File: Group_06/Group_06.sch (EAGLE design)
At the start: 18 parts, among them J1 POWER_JACKPTH_LOCK, U2 +12v

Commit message: CY8
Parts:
- added D1: BLUE, SparkFun-LED:LED-BLUE1206
- added J3: (no value), SparkFun-Connectors:CONN_06LOCK
- added R11: (no value), SparkFun-Resistors:RESISTORAXIAL-0.3
- added U$2: CY8CKIT-059_TARGET_3, CY8KIT-059:CY8CKIT-059_TARGET_3
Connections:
- new net MUX_A0/2.3C: U$2.P_1.7
- new net MUX_A1/2.3C: U$2.P_1.6
- new net MUX_A2/2.3C: U$2.P_1.5
- new net MUX_OUT/2.5C: U$2.P_1.4
- new net N$2: D1.C, R11.2
- new net N$3: D1.A, U$2.P_3.0
- new net N$4: J3.6, U$2.P_0.0
- new net N$5: J3.5, U$2.P_0.1
- new net N$6: J3.4, U$2.P_0.2
- new net N$7: J3.3, U$2.P_0.3
- new net N$8: J3.2, U$2.P_0.4
- new net N$9: J3.1, U$2.P_0.5
- net 5V: now also U$2.VDD, U$2.VDDIO
- net GND: now also R11.1, U$2.GND1, U$2.GND3
- net I2C_A0: now also U$2.P_2.5
- net I2C_A1: now also U$2.P_2.6
- net I2C_A2: now also U$2.P_2.7
- net I2C_SCL: now also U$2.P_12.0
- net I2C_SDA: now also U$2.P_12.1
- net PHOTO_OUT: now also U$2.P_3.7
- net TEMP_OUT: now also U$2.P_15.0

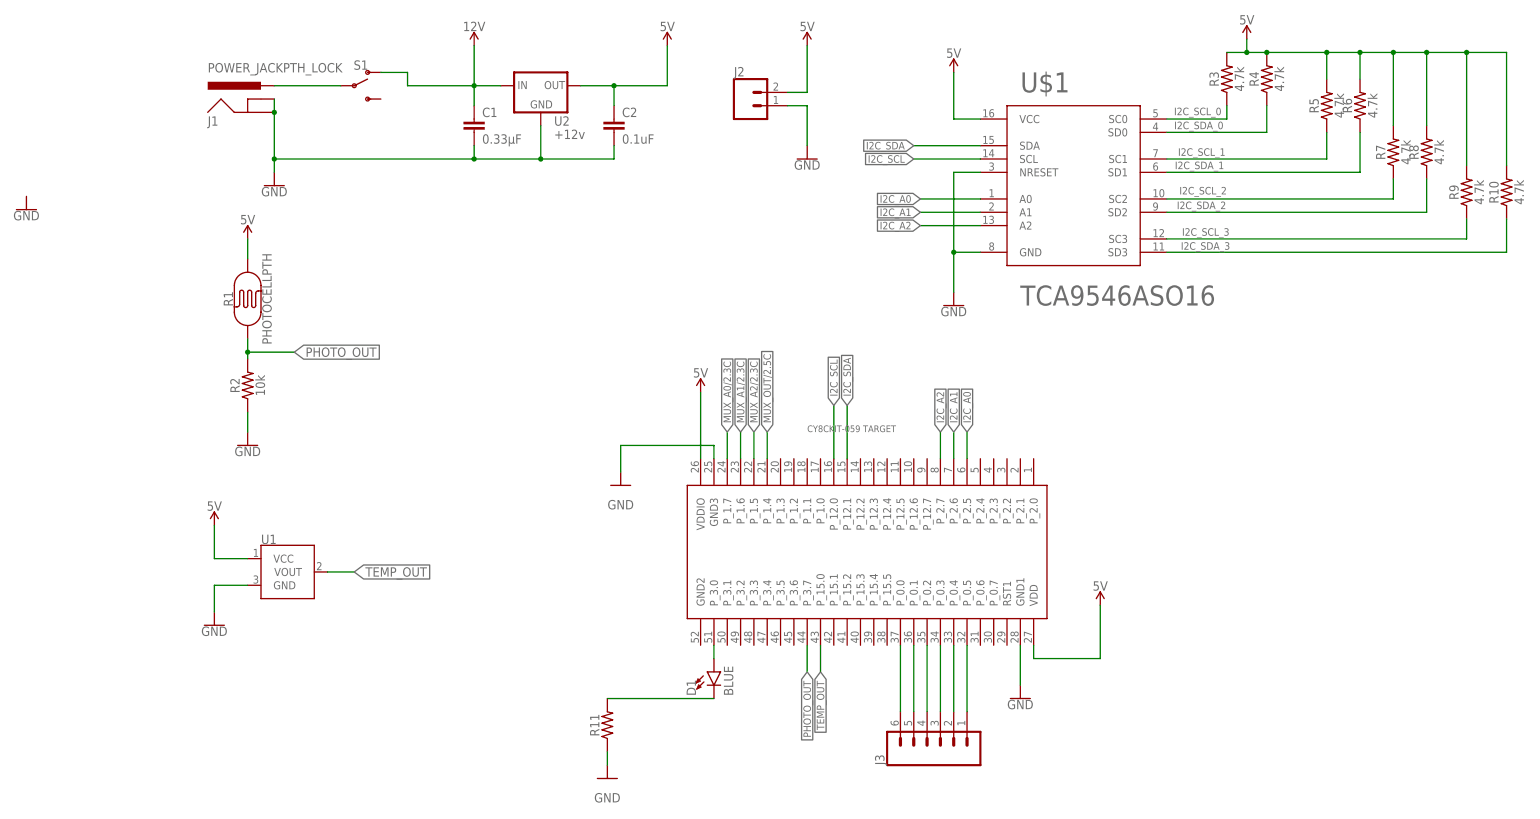
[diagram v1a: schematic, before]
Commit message: I2C_Connectors and Names
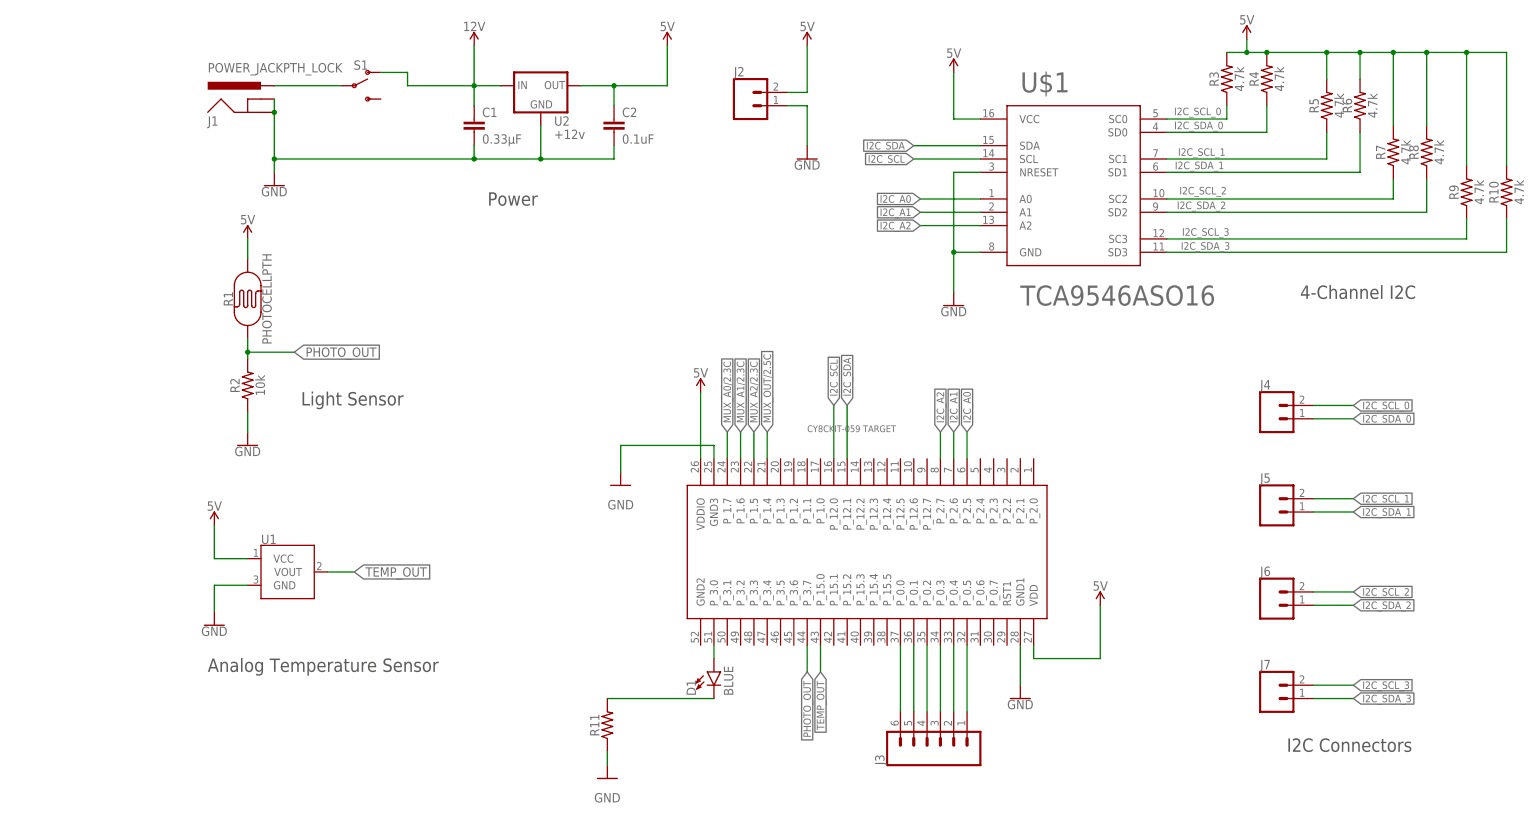
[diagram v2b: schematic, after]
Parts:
- added J4, J5, J6, J7: (no value), SparkFun-Connectors:CONN_02
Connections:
- net I2C_SCL_0: now also J4.2
- net I2C_SCL_1: now also J5.2
- net I2C_SCL_2: now also J6.2
- net I2C_SCL_3: now also J7.2
- net I2C_SDA_0: now also J4.1
- net I2C_SDA_1: now also J5.1
- net I2C_SDA_2: now also J6.1
- net I2C_SDA_3: now also J7.1
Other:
- note added: "4-Channel I2C"
- note added: "Analog Temperature Sensor"
- note added: "I2C Connectors"
- note added: "Light Sensor"
- note added: "Power"
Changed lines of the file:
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@@
 <part name="U$2" library="CY8KIT-059" deviceset="CY8CKIT-059_TARGET_3" device=""/>
 <part name="R11" library="SparkFun-Resistors" deviceset="RESISTOR" device="AXIAL-0.3" value=" "/>
-<part name="GND6" library="SparkFun-PowerSymbols" deviceset="GND" device=""/>
 <part name="GND7" library="SparkFun-PowerSymbols" deviceset="GND" device=""/>
 <part name="GND8" library="SparkFun-PowerSymbols" deviceset="GND" device=""/>
@@
 <part name="D1" library="SparkFun-LED" deviceset="LED-BLUE" device="1206" value="BLUE"/>
 <part name="J3" library="SparkFun-Connectors" deviceset="CONN_06" device="LOCK"/>
+<part name="J4" library="SparkFun-Connectors" deviceset="CONN_02" device=""/>
+<part name="J5" library="SparkFun-Connectors" deviceset="CONN_02" device=""/>
+<part name="J6" library="SparkFun-Connectors" deviceset="CONN_02" device=""/>
+<part name="J7" library="SparkFun-Connectors" deviceset="CONN_02" device=""/>
 </parts>
 <sheets>
 <sheet>
 <plain>
+<text x="223.52" y="35.56" size="2.54" layer="97">I2C Connectors</text>
+<text x="226.06" y="121.92" size="2.54" layer="97">4-Channel I2C</text>
+<text x="71.12" y="139.7" size="2.54" layer="97">Power</text>
+<text x="35.56" y="101.6" size="2.54" layer="97">Light Sensor</text>
+<text x="17.78" y="50.8" size="2.54" layer="97">Analog Temperature Sensor</text>
 </plain>
 <instances>
@@
 <attribute name="VALUE" x="92.964" y="40.64" size="1.778" layer="96" font="vector" rot="R90" align="top-center"/>
 </instance>
-<instance part="GND6" gate="1" x="-16.78295625" y="138.935128125" smashed="yes">
-<attribute name="VALUE" x="-16.78295625" y="138.681128125" size="1.778" layer="96" align="top-center"/>
-</instance>
 <instance part="GND7" gate="1" x="93.98" y="30.48" smashed="yes">
 <attribute name="VALUE" x="93.98" y="27.686" size="1.778" layer="96" align="top-center"/>
@@
 <attribute name="VALUE" x="167.386" y="33.02" size="1.778" layer="96" font="vector" rot="R90"/>
 <attribute name="NAME" x="146.812" y="33.02" size="1.778" layer="95" font="vector" rot="R90"/>
+</instance>
+<instance part="J4" gate="G$1" x="220.98" y="99.06" smashed="yes">
+<attribute name="VALUE" x="218.44" y="94.234" size="1.778" layer="96" font="vector"/>
+<attribute name="NAME" x="218.44" y="104.648" size="1.778" layer="95" font="vector"/>
+</instance>
+<instance part="J5" gate="G$1" x="220.98" y="81.28" smashed="yes">
+<attribute name="VALUE" x="218.44" y="76.454" size="1.778" layer="96" font="vector"/>
+<attribute name="NAME" x="218.44" y="86.868" size="1.778" layer="95" font="vector"/>
+</instance>
+<instance part="J6" gate="G$1" x="220.98" y="63.5" smashed="yes">
+<attribute name="VALUE" x="218.44" y="58.674" size="1.778" layer="96" font="vector"/>
+<attribute name="NAME" x="218.44" y="69.088" size="1.778" layer="95" font="vector"/>
+</instance>
+<instance part="J7" gate="G$1" x="220.98" y="45.72" smashed="yes">
+<attribute name="VALUE" x="218.44" y="40.894" size="1.778" layer="96" font="vector"/>
+<attribute name="NAME" x="218.44" y="51.308" size="1.778" layer="95" font="vector"/>
 </instance>
 </instances>
@@
 <label x="211.074" y="158.369" size="1.4224" layer="95" rot="R180"/>
 </segment>
+<segment>
+<pinref part="J4" gate="G$1" pin="2"/>
+<wire x1="228.6" y1="101.6" x2="236.22" y2="101.6" width="0.1524" layer="91"/>
+<label x="236.22" y="101.6" size="1.4224" layer="95" xref="yes"/>
+</segment>
 </net>
 <net name="I2C_SDA_0" class="0">
@@
 <label x="211.455" y="155.702" size="1.4224" layer="95" rot="R180"/>
 </segment>
+<segment>
+<pinref part="J4" gate="G$1" pin="1"/>
+<wire x1="228.6" y1="99.06" x2="236.22" y2="99.06" width="0.1524" layer="91"/>
+<label x="236.22" y="99.06" size="1.4224" layer="95" xref="yes"/>
+</segment>
 </net>
 <net name="I2C_SCL_1" class="0">
@@
 <label x="211.836" y="150.622" size="1.4224" layer="95" rot="R180"/>
 </segment>
+<segment>
+<pinref part="J5" gate="G$1" pin="2"/>
+<wire x1="228.6" y1="83.82" x2="236.22" y2="83.82" width="0.1524" layer="91"/>
+<label x="236.22" y="83.82" size="1.4224" layer="95" xref="yes"/>
+</segment>
 </net>
 <net name="I2C_SDA_1" class="0">
@@
 <label x="211.582" y="148.082" size="1.4224" layer="95" rot="R180"/>
 </segment>
+<segment>
+<pinref part="J5" gate="G$1" pin="1"/>
+<wire x1="228.6" y1="81.28" x2="236.22" y2="81.28" width="0.1524" layer="91"/>
+<label x="236.22" y="81.28" size="1.4224" layer="95" xref="yes"/>
+</segment>
 </net>
 <net name="I2C_SCL_2" class="0">
@@
 <label x="212.09" y="143.256" size="1.4224" layer="95" rot="R180"/>
 </segment>
+<segment>
+<pinref part="J6" gate="G$1" pin="2"/>
+<wire x1="228.6" y1="66.04" x2="236.22" y2="66.04" width="0.1524" layer="91"/>
+<label x="236.22" y="66.04" size="1.4224" layer="95" xref="yes"/>
+</segment>
 </net>
 <net name="I2C_SDA_2" class="0">
@@
 <label x="211.963" y="140.462" size="1.4224" layer="95" rot="R180"/>
 </segment>
+<segment>
+<pinref part="J6" gate="G$1" pin="1"/>
+<wire x1="228.6" y1="63.5" x2="236.22" y2="63.5" width="0.1524" layer="91"/>
+<label x="236.22" y="63.5" size="1.4224" layer="95" xref="yes"/>
+</segment>
 </net>
 <net name="I2C_SCL_3" class="0">
@@
 <label x="212.598" y="135.382" size="1.4224" layer="95" rot="R180"/>
 </segment>
+<segment>
+<pinref part="J7" gate="G$1" pin="2"/>
+<wire x1="228.6" y1="48.26" x2="236.22" y2="48.26" width="0.1524" layer="91"/>
+<label x="236.22" y="48.26" size="1.4224" layer="95" xref="yes"/>
+</segment>
 </net>
 <net name="I2C_SDA_3" class="0">
@@
 <label x="212.725" y="132.715" size="1.4224" layer="95" rot="R180"/>
 </segment>
-</net>
+<segment>
+<pinref part="J7" gate="G$1" pin="1"/>
+<wire x1="228.6" y1="45.72" x2="236.22" y2="45.72" width="0.1524" layer="91"/>
+<label x="236.22" y="45.72" size="1.4224" layer="95" xref="yes"/>
+</segment>
+</net>

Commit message: Adding TMUX1208
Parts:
- added C3: 0.1uF, SparkFun-Capacitors:0.1UF-KIT-EZ-50V-20%
- added J8: (no value), SparkFun-Connectors:CONN_08"
- added U$3: TMUX1208RSV, Group_06_Library:TMUX1208RSV
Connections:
- new net MUX_A0/1.3C: U$3.A0
- new net N$10: J8.8, U$3.S1
- new net N$11: J8.7, U$3.S2
- new net N$12: J8.6, U$3.S3
- new net N$13: J8.5, U$3.S4
- new net N$14: J8.4, U$3.S5
- new net N$15: J8.3, U$3.S6
- new net N$16: J8.2, U$3.S7
- new net N$17: J8.1, U$3.S8
- new net N$19: U$3.A1
- new net N$20: U$3.A2
- new net N$23: U$3.D
- net 5V: now also C3.1, U$3.EN, U$3.VDD
- net GND: now also C3.2, U$3.GND
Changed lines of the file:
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@@
 <part name="J6" library="SparkFun-Connectors" deviceset="CONN_02" device=""/>
 <part name="J7" library="SparkFun-Connectors" deviceset="CONN_02" device=""/>
+<part name="FRAME2" library="SparkFun-Aesthetics" deviceset="FRAME-A4L" device=""/>
+<part name="U$3" library="Group_06_Library" deviceset="TMUX1208" device="RSV"/>
+<part name="J8" library="SparkFun-Connectors" deviceset="CONN_08" device="&quot;"/>
+<part name="SUPPLY10" library="SparkFun-PowerSymbols" deviceset="5V" device=""/>
+<part name="SUPPLY11" library="SparkFun-PowerSymbols" deviceset="5V" device=""/>
+<part name="GND6" library="SparkFun-PowerSymbols" deviceset="GND" device=""/>
+<part name="C3" library="SparkFun-Capacitors" deviceset="0.1UF" device="-KIT-EZ-50V-20%" value="0.1uF"/>
 </parts>
 <sheets>
@@
 </segment>
 </net>
+</nets>
+</sheet>
+<sheet>
+<plain>
+</plain>
+<instances>
+<instance part="FRAME2" gate="G$1" x="0" y="0" smashed="yes">
+<attribute name="DRAWING_NAME" x="181.61" y="11.43" size="2.54" layer="94" font="vector"/>
+<attribute name="LAST_DATE_TIME" x="181.61" y="6.35" size="2.286" layer="94" font="vector"/>
+<attribute name="SHEET" x="195.58" y="1.27" size="2.54" layer="94" font="vector"/>
+<attribute name="DESIGNER" x="226.26" y="6.35" size="2.54" layer="94" font="vector"/>
+</instance>
+<instance part="U$3" gate="G$1" x="121.92" y="91.44" smashed="yes">
+<attribute name="NAME" x="112.522" y="121.666" size="3.81" layer="95"/>
+<attribute name="VALUE" x="104.14" y="58.42" size="3.81" layer="95"/>
+</instance>
+<instance part="J8" gate="G$1" x="81.28" y="104.14" smashed="yes">
+<attribute name="VALUE" x="76.2" y="91.694" size="1.778" layer="96" font="vector"/>
+<attribute name="NAME" x="76.2" y="117.348" size="1.778" layer="95" font="vector"/>
+</instance>
+<instance part="SUPPLY10" gate="G$1" x="147.32" y="78.74" smashed="yes">
+<attribute name="VALUE" x="147.32" y="81.534" size="1.778" layer="96" align="bottom-center"/>
+</instance>
+<instance part="SUPPLY11" gate="G$1" x="147.32" y="121.92" smashed="yes">
+<attribute name="VALUE" x="147.32" y="124.714" size="1.778" layer="96" align="bottom-center"/>
+</instance>
+<instance part="GND6" gate="1" x="147.32" y="60.96" smashed="yes">
+<attribute name="VALUE" x="147.32" y="60.706" size="1.778" layer="96" align="top-center"/>
+</instance>
+<instance part="C3" gate="G$1" x="180.34" y="91.44" smashed="yes">
+<attribute name="NAME" x="181.864" y="94.361" size="1.778" layer="95" font="vector"/>
+<attribute name="VALUE" x="181.864" y="89.281" size="1.778" layer="96" font="vector"/>
+</instance>
+</instances>
+<busses>
+</busses>
+<nets>
+<net name="N$10" class="0">
+<segment>
+<pinref part="J8" gate="G$1" pin="8"/>
+<pinref part="U$3" gate="G$1" pin="S1"/>
+<wire x1="86.36" y1="114.3" x2="104.14" y2="114.3" width="0.1524" layer="91"/>
+</segment>
+</net>
+<net name="N$11" class="0">
+<segment>
+<pinref part="J8" gate="G$1" pin="7"/>
+<pinref part="U$3" gate="G$1" pin="S2"/>
+<wire x1="86.36" y1="111.76" x2="104.14" y2="111.76" width="0.1524" layer="91"/>
+</segment>
+</net>
+<net name="N$12" class="0">
+<segment>
+<pinref part="J8" gate="G$1" pin="6"/>
+<pinref part="U$3" gate="G$1" pin="S3"/>
+<wire x1="86.36" y1="109.22" x2="104.14" y2="109.22" width="0.1524" layer="91"/>
+</segment>
+</net>
+<net name="N$13" class="0">
+<segment>
+<pinref part="J8" gate="G$1" pin="5"/>
+<pinref part="U$3" gate="G$1" pin="S4"/>
+<wire x1="86.36" y1="106.68" x2="104.14" y2="106.68" width="0.1524" layer="91"/>
+</segment>
+</net>
+<net name="N$14" class="0">
+<segment>
+<pinref part="J8" gate="G$1" pin="4"/>
+<pinref part="U$3" gate="G$1" pin="S5"/>
+<wire x1="86.36" y1="104.14" x2="104.14" y2="104.14" width="0.1524" layer="91"/>
+</segment>
+</net>
+<net name="N$15" class="0">
+<segment>
+<pinref part="J8" gate="G$1" pin="3"/>
+<pinref part="U$3" gate="G$1" pin="S6"/>
+<wire x1="86.36" y1="101.6" x2="104.14" y2="101.6" width="0.1524" layer="91"/>
+</segment>
+</net>
+<net name="N$16" class="0">
+<segment>
+<pinref part="J8" gate="G$1" pin="2"/>
+<pinref part="U$3" gate="G$1" pin="S7"/>
+<wire x1="86.36" y1="99.06" x2="104.14" y2="99.06" width="0.1524" layer="91"/>
+</segment>
+</net>
+<net name="N$17" class="0">
+<segment>
+<pinref part="J8" gate="G$1" pin="1"/>
+<pinref part="U$3" gate="G$1" pin="S8"/>
+<wire x1="86.36" y1="96.52" x2="104.14" y2="96.52" width="0.1524" layer="91"/>
+</segment>
+</net>
+<net name="MUX_A0/1.3C" class="0">
+<segment>
+<pinref part="U$3" gate="G$1" pin="A0"/>
+<wire x1="104.14" y1="73.66" x2="83.82" y2="73.66" width="0.1524" layer="91"/>
+</segment>
+</net>
+<net name="N$19" class="0">
+<segment>
+<pinref part="U$3" gate="G$1" pin="A1"/>
+<wire x1="104.14" y1="71.12" x2="83.82" y2="71.12" width="0.1524" layer="91"/>
+</segment>
+</net>
+<net name="N$20" class="0">
+<segment>
+<pinref part="U$3" gate="G$1" pin="A2"/>
+<wire x1="104.14" y1="68.58" x2="83.82" y2="68.58" width="0.1524" layer="91"/>
+</segment>
+</net>
+<net name="GND" class="0">
+<segment>
+<pinref part="U$3" gate="G$1" pin="GND"/>
+<wire x1="139.7" y1="68.58" x2="147.32" y2="68.58" width="0.1524" layer="91"/>
+<pinref part="GND6" gate="1" pin="GND"/>
+<wire x1="147.32" y1="68.58" x2="147.32" y2="63.5" width="0.1524" layer="91"/>
+<pinref part="C3" gate="G$1" pin="2"/>
+<wire x1="147.32" y1="68.58" x2="180.34" y2="68.58" width="0.1524" layer="91"/>
+<wire x1="180.34" y1="68.58" x2="180.34" y2="88.9" width="0.1524" layer="91"/>
+<junction x="147.32" y="68.58"/>
+</segment>
+</net>
+<net name="5V" class="0">
+<segment>
+<pinref part="U$3" gate="G$1" pin="EN"/>
+<pinref part="SUPPLY10" gate="G$1" pin="5V"/>
+<wire x1="139.7" y1="71.12" x2="147.32" y2="71.12" width="0.1524" layer="91"/>
+<wire x1="147.32" y1="71.12" x2="147.32" y2="78.74" width="0.1524" layer="91"/>
+</segment>
+<segment>
+<pinref part="C3" gate="G$1" pin="1"/>
+<pinref part="U$3" gate="G$1" pin="VDD"/>
+<wire x1="180.34" y1="96.52" x2="180.34" y2="114.3" width="0.1524" layer="91"/>
+<wire x1="180.34" y1="114.3" x2="147.32" y2="114.3" width="0.1524" layer="91"/>
+<pinref part="SUPPLY11" gate="G$1" pin="5V"/>
+<wire x1="147.32" y1="114.3" x2="139.7" y2="114.3" width="0.1524" layer="91"/>
+<wire x1="147.32" y1="121.92" x2="147.32" y2="114.3" width="0.1524" layer="91"/>
+<junction x="147.32" y="114.3"/>
+</segment>
+</net>
+<net name="N$23" class="0">
+<segment>
+<pinref part="U$3" gate="G$1" pin="D"/>
+<wire x1="139.7" y1="91.44" x2="144.78" y2="91.44" width="0.1524" layer="91"/>
+</segment>
+</net>
